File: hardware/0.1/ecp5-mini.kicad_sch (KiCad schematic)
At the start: 21 parts, among them U1 ECP5U_12_CABGA256

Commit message: decoupling down + outer pins fanned out
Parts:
- removed C21, C22, C27, C28, C33, C34: 100n, Capacitor_SMD:C_0402_1005Metric, symbol Device:C
- removed C24, C35, C36: 470n, Capacitor_SMD:C_0402_1005Metric, symbol Device:C
- C23, C29, C30: value 470n -> 4u7
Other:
- moved on the sheet: C23, C29, C30

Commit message: cleaning up schematic
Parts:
- added J? (x2): S7 Mini, josh-connectors:ECP5-Mini-Edge-20x2.54-40x1.27, symbol Connector:Conn_01x40_Male
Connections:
- net +3V3: now also J?.19 (Pin_19), J?.19 (Pin_19)
- net GND: now also J?.10 (Pin_10), J?.10 (Pin_10), J?.20 (Pin_20), J?.20 (Pin_20), J?.29 (Pin_29), J?.29 (Pin_29), J?.30 (Pin_30), J?.30 (Pin_30), J?.40 (Pin_40), J?.40 (Pin_40), J?.9 (Pin_9), J?.9 (Pin_9)
- new net +5V: J?.39 (Pin_39), J?.39 (Pin_39)
- new net PORT_A0: J?.1 (Pin_1)
- new net PORT_A1: J?.3 (Pin_3)
- new net PORT_A2: J?.5 (Pin_5)
- new net PORT_A3: J?.7 (Pin_7)
- new net PORT_A4: J?.2 (Pin_2)
- new net PORT_A5: J?.4 (Pin_4)
- new net PORT_A6: J?.6 (Pin_6)
- new net PORT_A7: J?.8 (Pin_8)
- new net PORT_B0: J?.11 (Pin_11)
- new net PORT_B1: J?.13 (Pin_13)
- new net PORT_B2: J?.15 (Pin_15)
- new net PORT_B3: J?.17 (Pin_17)
- new net PORT_B4: J?.12 (Pin_12)
- new net PORT_B5: J?.14 (Pin_14)
- new net PORT_B6: J?.16 (Pin_16)
- new net PORT_B7: J?.18 (Pin_18)
- new net PORT_C0: J?.21 (Pin_21)
- new net PORT_C1: J?.23 (Pin_23)
- new net PORT_C2: J?.25 (Pin_25)
- new net PORT_C3: J?.27 (Pin_27)
- new net PORT_C4: J?.22 (Pin_22)
- new net PORT_C5: J?.24 (Pin_24)
- new net PORT_C6: J?.26 (Pin_26)
- new net PORT_C7: J?.28 (Pin_28)
- new net PORT_D0: J?.31 (Pin_31)
- new net PORT_D1: J?.33 (Pin_33)
- new net PORT_D2: J?.35 (Pin_35)
- new net PORT_D3: J?.37 (Pin_37)
- new net PORT_D4: J?.32 (Pin_32)
- new net PORT_D5: J?.34 (Pin_34)
- new net PORT_D6: J?.36 (Pin_36)
- new net PORT_D7: J?.38 (Pin_38)
- new net PORT_E0: J?.31 (Pin_31)
- new net PORT_E1: J?.33 (Pin_33)
- new net PORT_E2: J?.35 (Pin_35)
- new net PORT_E3: J?.37 (Pin_37)
- new net PORT_E4: J?.32 (Pin_32)
- new net PORT_E5: J?.34 (Pin_34)
- new net PORT_E6: J?.36 (Pin_36)
- new net PORT_E7: J?.38 (Pin_38)
- new net PORT_F0: J?.21 (Pin_21)
- new net PORT_F1: J?.23 (Pin_23)
- new net PORT_F2: J?.25 (Pin_25)
- new net PORT_F3: J?.27 (Pin_27)
- new net PORT_F4: J?.22 (Pin_22)
- new net PORT_F5: J?.24 (Pin_24)
- new net PORT_F6: J?.26 (Pin_26)
- new net PORT_F7: J?.28 (Pin_28)
- new net PORT_G0: J?.1 (Pin_1), J?.11 (Pin_11)
- new net PORT_G1: J?.13 (Pin_13), J?.3 (Pin_3)
- new net PORT_G2: J?.15 (Pin_15), J?.5 (Pin_5)
- new net PORT_G3: J?.17 (Pin_17), J?.7 (Pin_7)
- new net PORT_G4: J?.12 (Pin_12), J?.2 (Pin_2)
- new net PORT_G5: J?.14 (Pin_14), J?.4 (Pin_4)
- new net PORT_G6: J?.16 (Pin_16), J?.6 (Pin_6)
- new net PORT_G7: J?.18 (Pin_18), J?.8 (Pin_8)
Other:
- removed sheet Board IO
- removed sheet Hyperram / Micro SD
- added sheet SD / Hyperram (storage.kicad_sch)
- sheet FPGA Config ports: added {USB[0..2]}; removed USB
- note added: "Breakout Pins"
- note added: "ECP5 Mini"
- note added: "Following Black Mesa Lab's "S7 Mini" form factor"
- note added: "IO Banks"
- note added: "Sub Sheets"
- moved on the sheet: C19, C20, C23, C25, C26, C29, C30, C31, C32, LOGO1, LOGO2, U1B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

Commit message: layout ++
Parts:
- added C14: 100n, Capacitor_SMD:C_0402_1005Metric, symbol Device:C
- added X1: DSC6101CI2A-016, josh-oscillators:CDFN_3.2x2.5mm_XO, symbol josh-oscillator:DSC6101CI1A
- gave numbers to parts that had none: 2
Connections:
- net +3V3: now also C14.1, X1.1 (OE/STBY), X1.4 (VDD)
- net GND: now also C14.2, X1.2 (GND)
- net CLK_16MHZ: now reaches U1.A7 (PT29A/+/PCLKT0_0)
- net CLK_16MHZ: now also X1.3 (OUT)
- net HR_nCS: now reaches U1.N3 (PL35D/-/LDQ32)
- net HR_CK_P: now reaches U1.P1 (PL35A/+/HS/LDQ32)
- net HR_CK_N: now reaches U1.P2 (PL32B/-/HS/LDQSN32)
- net HR_DQ4: now reaches U1.P3 (PL38B/-/HS/LDQ44)
- net HR_DQ7: now reaches U1.P5 (PL47D/-/LLC_GPLL0C_IN/LDQ44)
- net HR_nRST: now reaches U1.R1 (PL35B/-/VREF1_6/HS/LDQ32)
- net HR_RWDS: now reaches U1.R2 (PL38C/+/LDQ44)
- net HR_DQ2: now reaches U1.R3 (PL41B/-/HS/LDQ44)
- net HR_DQ1: now reaches U1.R4 (PL41C/+/LDQ44)
- net HR_DQ6: now reaches U1.R5 (PL44A/+/HS/LDQS44)
- net HR_DQ0: now reaches U1.T2 (PL38D/-/LDQ44)
- net HR_DQ3: now reaches U1.T3 (PL41D/-/LDQ44)
- net HR_DQ5: now reaches U1.T4 (PL44B/-/HS/LDQSN44)
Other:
- sheet FPGA Config ports: added {USB}; removed {USB[0..2]}
- sheet SD / Hyperram ports: added {HYPERRAM}, {SD}; removed {Hyperram[0..12]}, {SD[0..7]}
- note added: "Sub Sections"
- note removed: "Sub Sheets"

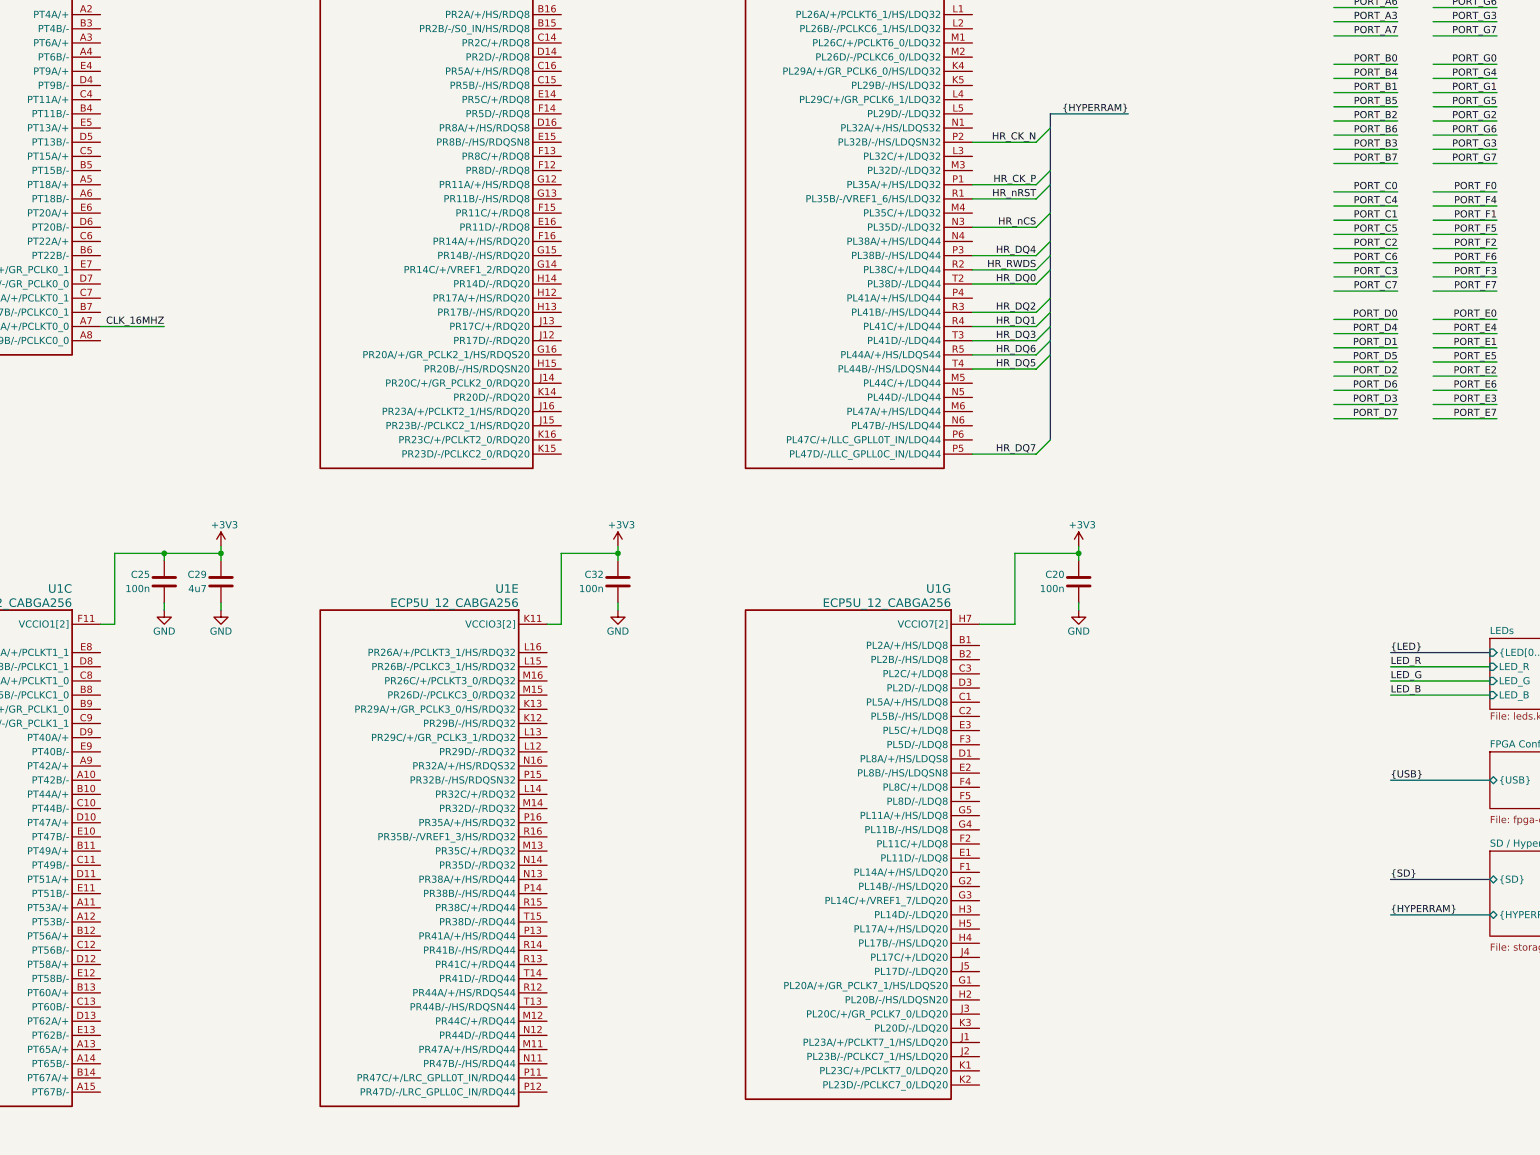
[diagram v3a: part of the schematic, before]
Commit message: hyperram routed
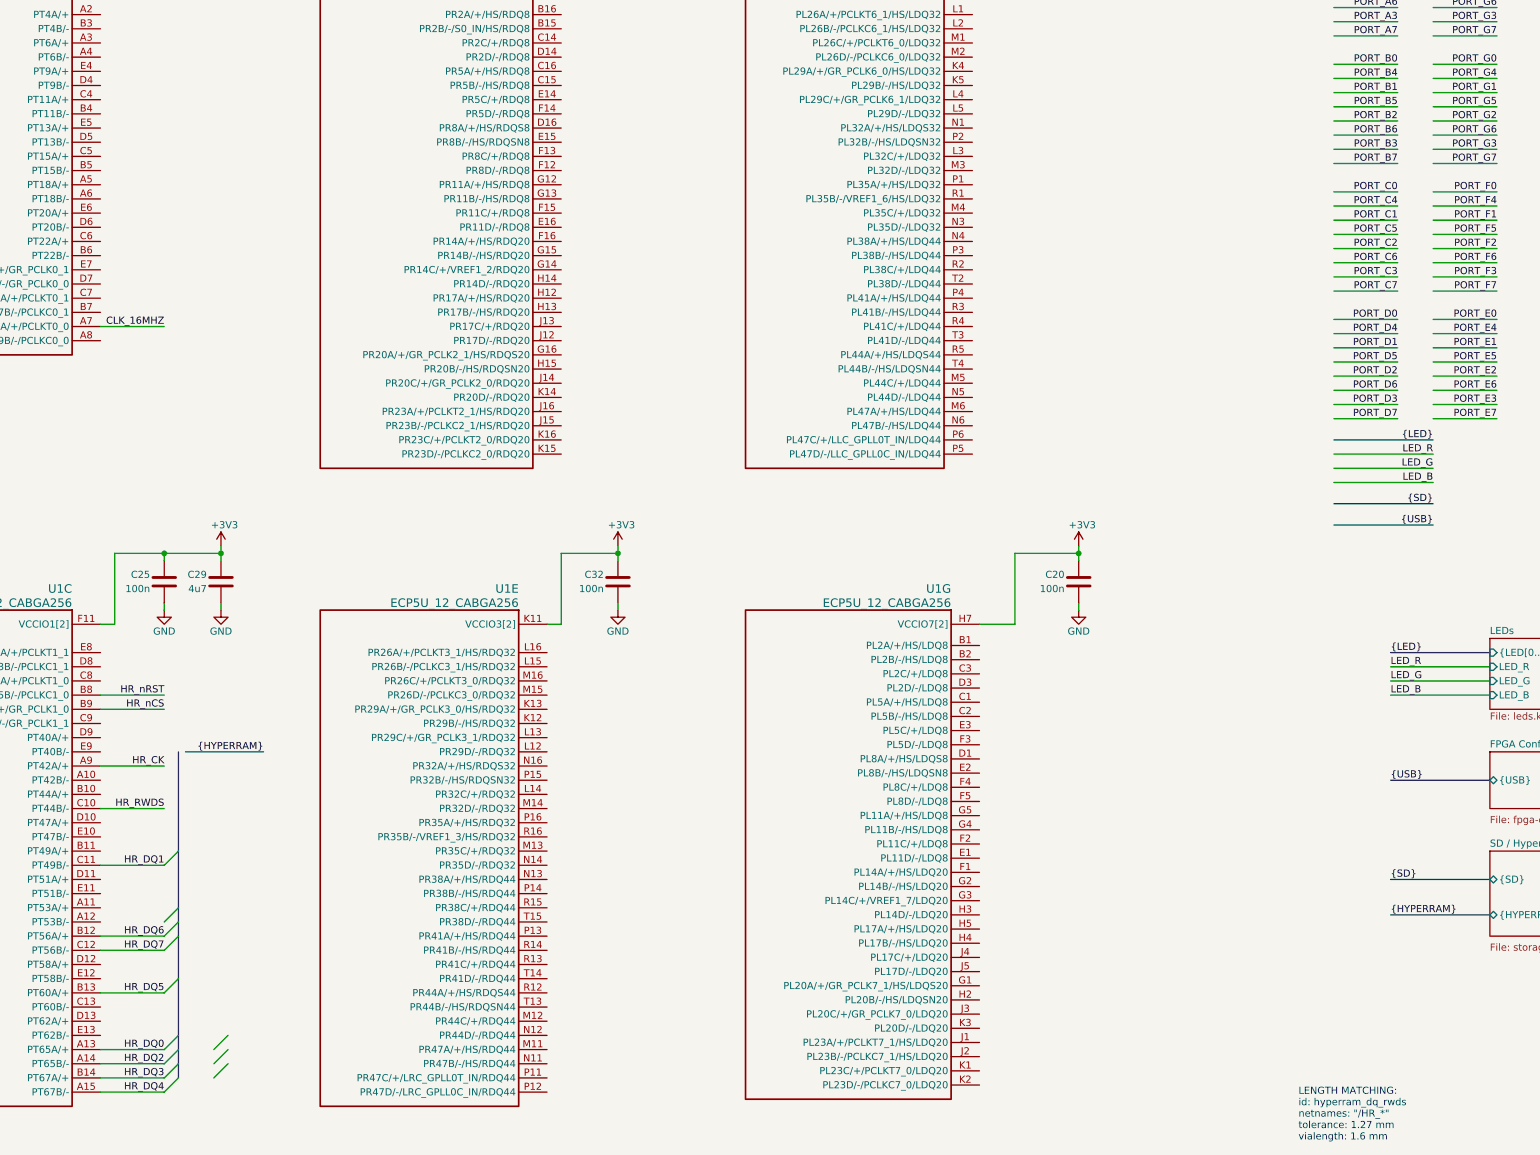
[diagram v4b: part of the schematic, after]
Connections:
- net HR_DQ0: now also U1.A13 (PT65A/+); no longer U1.T2 (PL38D/-/LDQ44)
- net HR_DQ1: now also U1.C11 (PT49B/-); no longer U1.R4 (PL41C/+/LDQ44)
- net HR_DQ2: now also U1.A14 (PT65B/-); no longer U1.R3 (PL41B/-/HS/LDQ44)
- net HR_DQ3: now also U1.B14 (PT67A/+); no longer U1.T3 (PL41D/-/LDQ44)
- net HR_DQ4: now also U1.A15 (PT67B/-); no longer U1.P3 (PL38B/-/HS/LDQ44)
- net HR_DQ5: now also U1.B13 (PT60A/+); no longer U1.T4 (PL44B/-/HS/LDQSN44)
- net HR_DQ6: now also U1.B12 (PT56A/+); no longer U1.R5 (PL44A/+/HS/LDQS44)
- net HR_DQ7: now also U1.C12 (PT56B/-); no longer U1.P5 (PL47D/-/LLC_GPLL0C_IN/LDQ44)
- net HR_RWDS: now also U1.C10 (PT44B/-); no longer U1.R2 (PL38C/+/LDQ44)
- net HR_nCS: now also U1.B9 (PT38A/+/GR_PCLK1_0); no longer U1.N3 (PL35D/-/LDQ32)
- net HR_nRST: now also U1.B8 (PT35B/-/PCLKC1_0); no longer U1.R1 (PL35B/-/VREF1_6/HS/LDQ32)
- net HR_CK: now reaches U1.A9 (PT42A/+)
- net HR_CK_N: no longer names the net of U1.P2 (PL32B/-/HS/LDQSN32)
- net HR_CK_P: no longer names the net of U1.P1 (PL35A/+/HS/LDQ32)
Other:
- note added: "LENGTH MATCHING: id: hyperram_dq_rwds netnames: "/HR_*" tolerance: 1.27 mm vialength: 1.6 mm"

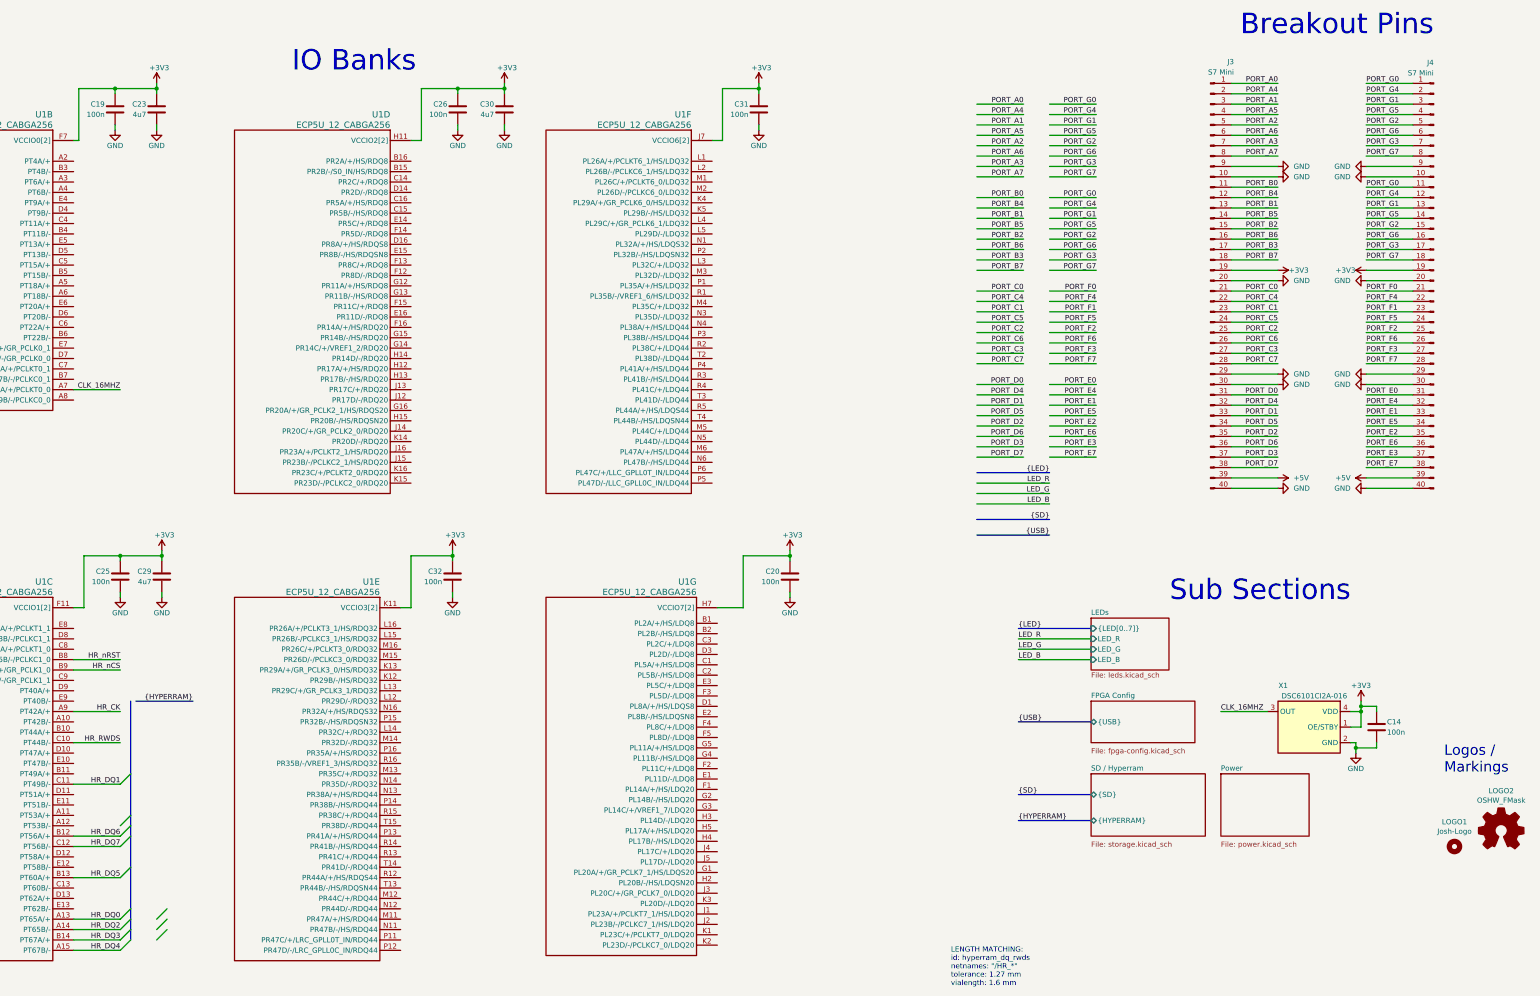
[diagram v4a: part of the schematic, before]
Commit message: half IO laid out
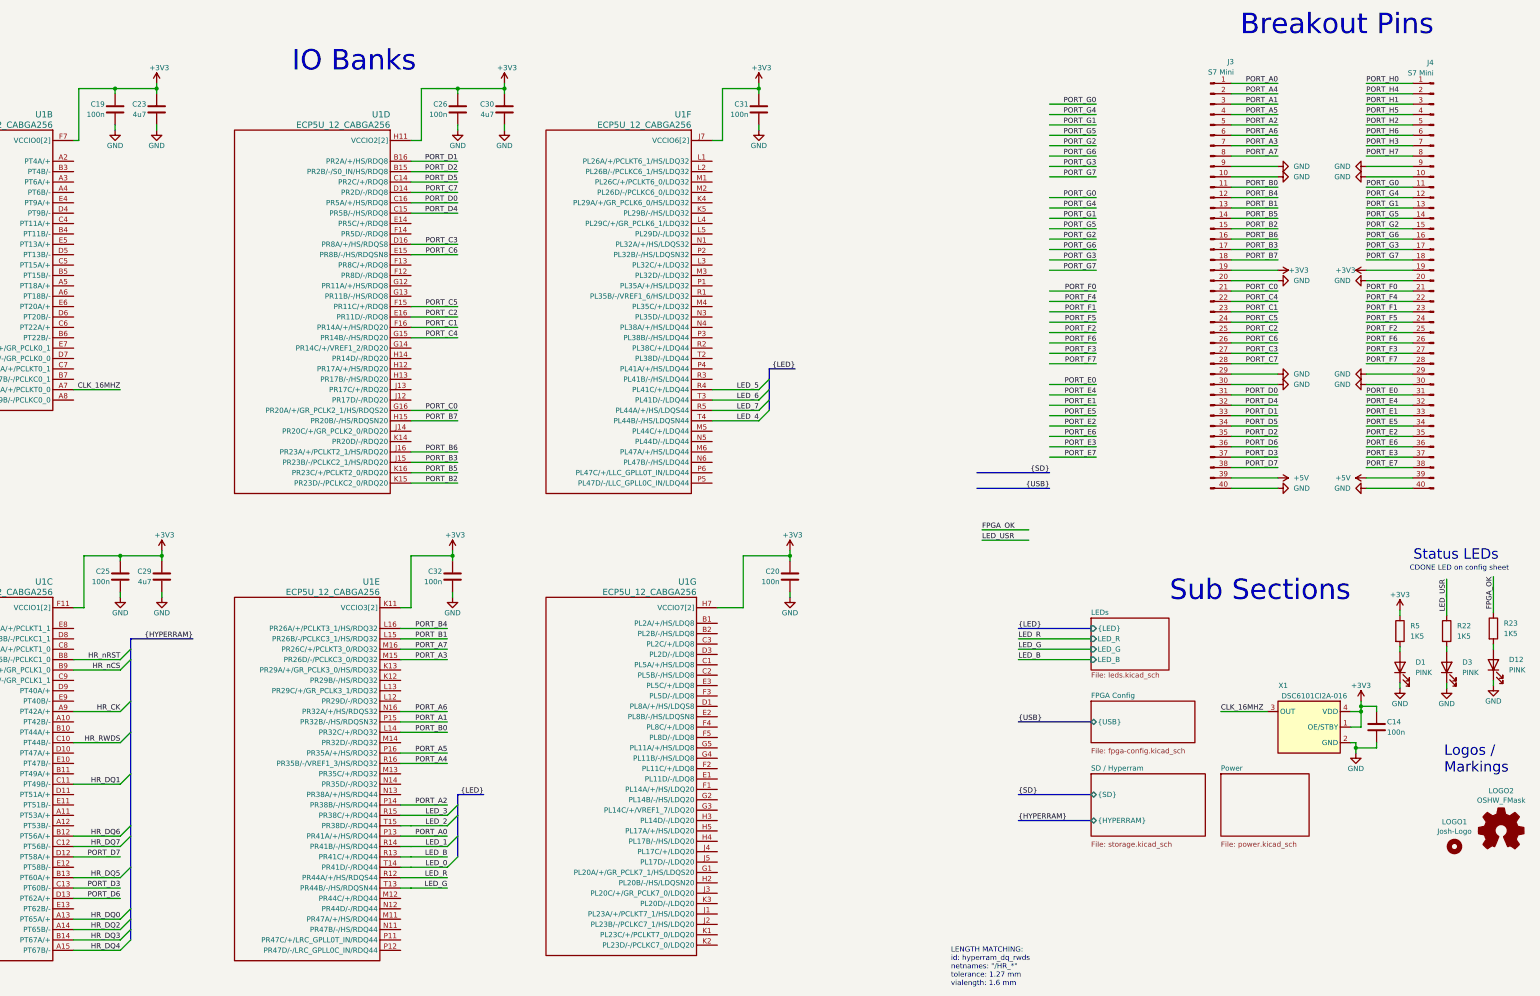
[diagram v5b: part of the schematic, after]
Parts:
- added D1, D12, D3: PINK, LED_SMD:LED_0603_1608Metric, symbol Device:LED
- added R22, R23, R5: 1K5, Resistor_SMD:R_0402_1005Metric, symbol Device:R
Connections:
- net +3V3: now also R5.1
- net GND: now also D1.1 (K), D12.1 (K), D3.1 (K)
- net LED_B: now also U1.R13 (PR41C/+/RDQ44)
- net LED_G: now also U1.T13 (PR44B/-/HS/RDQSN44)
- net LED_R: now also U1.R12 (PR44A/+/HS/RDQS44)
- net PORT_A0: now also U1.P13 (PR41A/+/HS/RDQ44)
- net PORT_A1: now also U1.P15 (PR32B/-/HS/RDQSN32)
- net PORT_A2: now also U1.P14 (PR38B/-/HS/RDQ44)
- net PORT_A3: now also U1.M15 (PR26D/-/PCLKC3_0/RDQ32)
- net PORT_A4: now also U1.R16 (PR35B/-/VREF1_3/HS/RDQ32)
- net PORT_A5: now also U1.P16 (PR35A/+/HS/RDQ32)
- net PORT_A6: now also U1.N16 (PR32A/+/HS/RDQS32)
- net PORT_A7: now also U1.M16 (PR26C/+/PCLKT3_0/RDQ32)
- net PORT_B0: now also U1.L14 (PR32C/+/RDQ32)
- net PORT_B1: now also U1.L15 (PR26B/-/PCLKC3_1/HS/RDQ32)
- net PORT_B2: now also U1.K15 (PR23D/-/PCLKC2_0/RDQ20)
- net PORT_B3: now also U1.J15 (PR23B/-/PCLKC2_1/HS/RDQ20)
- net PORT_B4: now also U1.L16 (PR26A/+/PCLKT3_1/HS/RDQ32)
- net PORT_B5: now also U1.K16 (PR23C/+/PCLKT2_0/RDQ20)
- net PORT_B6: now also U1.J16 (PR23A/+/PCLKT2_1/HS/RDQ20)
- net PORT_B7: now also U1.H15 (PR20B/-/HS/RDQSN20)
- net PORT_C0: now also U1.G16 (PR20A/+/GR_PCLK2_1/HS/RDQS20)
- net PORT_C1: now also U1.F16 (PR14A/+/HS/RDQ20)
- net PORT_C2: now also U1.E16 (PR11D/-/RDQ8)
- net PORT_C3: now also U1.D16 (PR8A/+/HS/RDQS8)
- net PORT_C4: now also U1.G15 (PR14B/-/HS/RDQ20)
- net PORT_C5: now also U1.F15 (PR11C/+/RDQ8)
- net PORT_C6: now also U1.E15 (PR8B/-/HS/RDQSN8)
- net PORT_C7: now also U1.D14 (PR2D/-/RDQ8)
- net PORT_D0: now also U1.C16 (PR5A/+/HS/RDQ8)
- net PORT_D1: now also U1.B16 (PR2A/+/HS/RDQ8)
- net PORT_D2: now also U1.B15 (PR2B/-/S0_IN/HS/RDQ8)
- net PORT_D3: now also U1.C13 (PT60B/-)
- net PORT_D4: now also U1.C15 (PR5B/-/HS/RDQ8)
- net PORT_D5: now also U1.C14 (PR2C/+/RDQ8)
- net PORT_D6: now also U1.D13 (PT62A/+)
- net PORT_D7: now also U1.D12 (PT58A/+)
- net PORT_G0: no longer J4.1 (Pin_1)
- net PORT_G1: no longer J4.3 (Pin_3)
- net PORT_G2: no longer J4.5 (Pin_5)
- net PORT_G3: no longer J4.7 (Pin_7)
- net PORT_G4: no longer J4.2 (Pin_2)
- net PORT_G5: no longer J4.4 (Pin_4)
- net PORT_G6: no longer J4.6 (Pin_6)
- net PORT_G7: no longer J4.8 (Pin_8)
- net LED_1: now reaches U1.R14 (PR41B/-/HS/RDQ44)
- net LED_3: now reaches U1.R15 (PR38C/+/RDQ44)
- net LED_0: now reaches U1.T14 (PR41D/-/RDQ44)
- net LED_2: now reaches U1.T15 (PR38D/-/RDQ44)
- net LED_5: now reaches U1.R4 (PL41C/+/LDQ44)
- net LED_7: now reaches U1.R5 (PL44A/+/HS/LDQS44)
- net LED_6: now reaches U1.T3 (PL41D/-/LDQ44)
- net LED_4: now reaches U1.T4 (PL44B/-/HS/LDQSN44)
- new net: D12.2 (A), R23.2
- new net: D1.2 (A), R5.2
- new net: D3.2 (A), R22.2
- new net FPGA_OK: R23.1
- new net LED_USR: R22.1
- new net PORT_H0: J4.1 (Pin_1)
- new net PORT_H1: J4.3 (Pin_3)
- new net PORT_H2: J4.5 (Pin_5)
- new net PORT_H3: J4.7 (Pin_7)
- new net PORT_H4: J4.2 (Pin_2)
- new net PORT_H5: J4.4 (Pin_4)
- new net PORT_H6: J4.6 (Pin_6)
- new net PORT_H7: J4.8 (Pin_8)
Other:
- sheet LEDs ports: added {LED}; removed {LED[0..7]}
- note added: "CDONE LED on config sheet"
- note added: "Status LEDs"
